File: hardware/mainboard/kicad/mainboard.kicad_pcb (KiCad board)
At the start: 4 copper layers, 54 x 120 mm, 134 parts, among them J1 XT30PW-M, J10 J_PYRO2, J11 J_GPS, J12 J_QWIIC, J13 J_CAM, J14 J_LED, J15 J_EXP, J2 J_BAT1, J3 J_SW, J4 J_ARM, J5 J_SERVO1, J6 J_SERVO2, J7 J_SERVO3, J8 J_MOT, J9 J_PYRO1, Q1 AO3401A, Q2 AO3401A, Q3 AO3400A, Q4 AO3400A, Q5 AO3400A, U1 TPS563201DDCR, U10 E22-400T22S, U2 TPS63070RNMR, U3 AP2112K-3.3TRG1, U4 ICM-42688-P, U5 BMP390, U6 INA219AIDR, U7 DRV8833PWPR, U8 74AHCT1G125, U9 74AHCT1G125

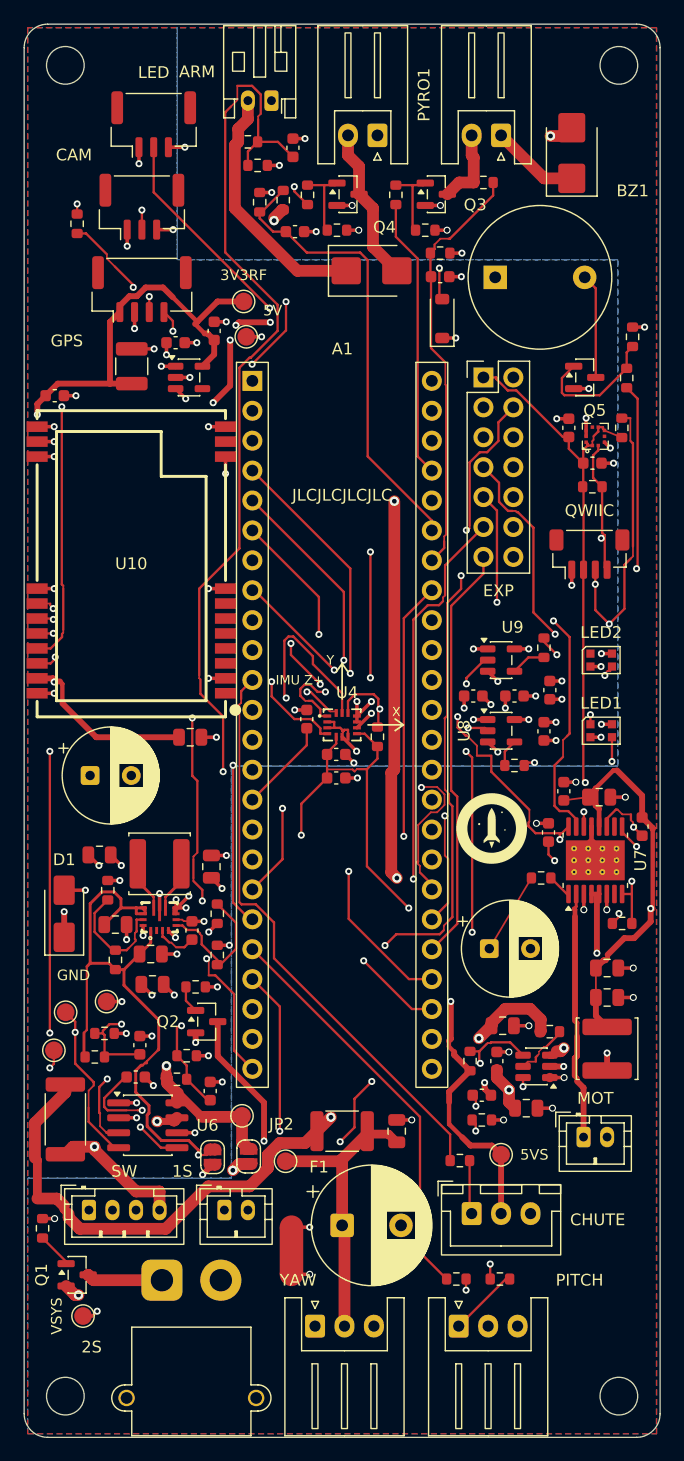
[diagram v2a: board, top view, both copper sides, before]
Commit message: Mainboard rev B1: Review A1-A8 und Entscheidungen E1-E10 eingearbeitet, 2S-Pfad als F.Cu-Flaechen, 28 Verbindungen offen
Schaltung (circuit.py, ERC 0, Netzliste gegen README §4 OK): Hold-up hinter D1, EN-Teiler 330k/115k,
P-FET-Lastschalter je Akku, Polyfuse je Akku, Kelvin-Shunt mit INA239 an SPI1, BMP390 an SPI1,
74HC138/74HC4051 mit gemeinsamer Adresse, J_STACK 2x10 mit LDO 3V3_EXP, 1S-Lader MCP73831,
J_CHG2, vier Pyro-Kanaele (3/4 DNP), vierter Servo, alle Servos und Rollmotor an VSERVO,
3V3_SENS, eine WS2812B-Kette, Summer Pin 37, E22 NRST Pin 6; 166 Bauteile.

Platine (gen_pcb.py): neue Platzierung, 2S-Pfad, Pyro-Ausgaenge und VSYS_IN als F.Cu-Flaechen mit
Sperrflaechen fuer Freerouting, Strom-Klasse nur F.Cu, IMU-Zone 5 mm, patch mit Umweg ueber In2.
DRC 0 Fehler, Paritaet 0, kein 2S-Netz auf In2; 28 offene Verbindungen, Liste in kicad/README.md §5.5.
Spezifikation README.md und kicad/README.md auf B1 nachgezogen, review_check_layout.py fuer B1.

Co-Authored-By: Claude Opus 5.5 <noreply@anthropic.com>
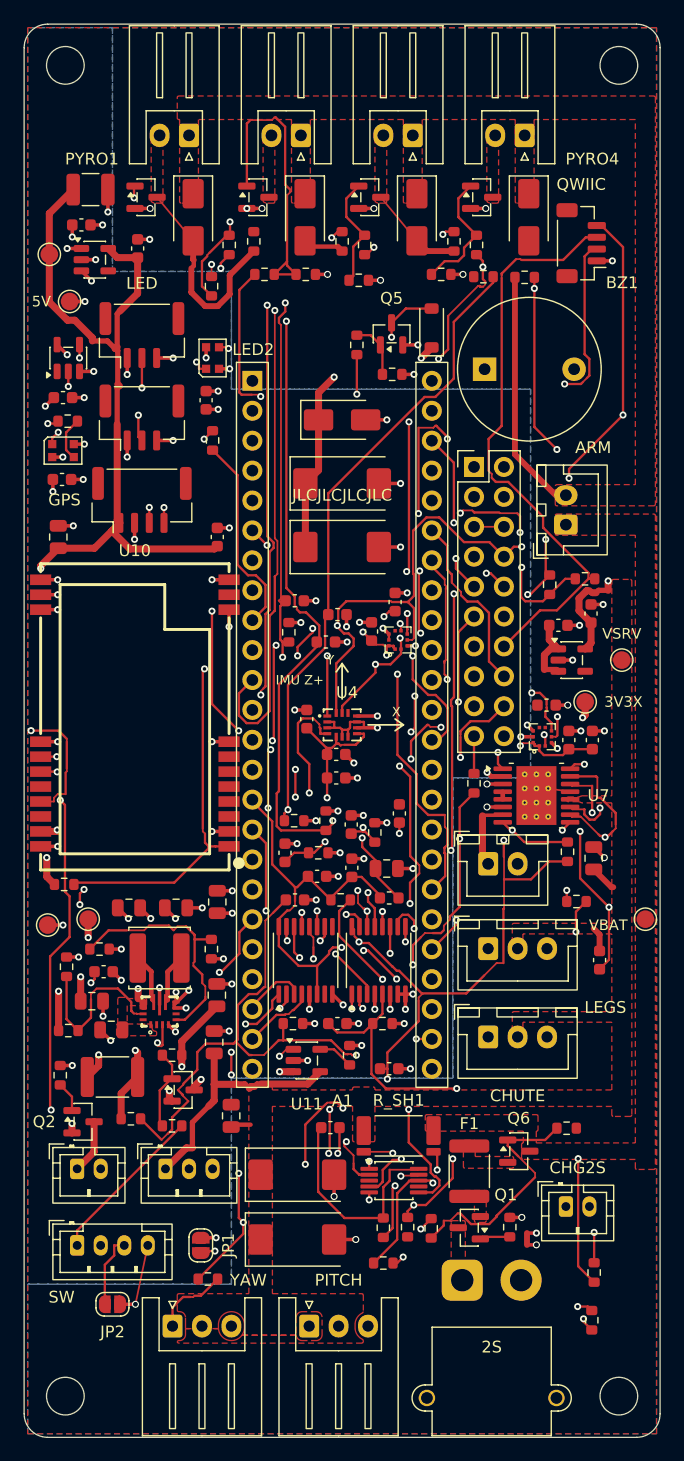
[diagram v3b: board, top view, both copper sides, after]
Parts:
- removed L1: 2.2u Isat>=4A, Inductor_SMD:L_Changjiang_FNR5040S
- removed TP8: SDA, TestPoint:TestPoint_Pad_D1.5mm
- removed TP9: SCL, TestPoint:TestPoint_Pad_D1.5mm
- removed U1: TPS563201DDCR, Package_TO_SOT_SMD:SOT-23-6
- removed U9: 74AHCT1G125, Package_TO_SOT_SMD:SOT-23-5
- added C41: 100n, Capacitor_SMD:C_0603_1608Metric, F.Cu at (125.6, 102.5)
- added C42: 100n, Capacitor_SMD:C_0603_1608Metric, F.Cu at (123.0, 99.0)
- added C43: 100n, Capacitor_SMD:C_0603_1608Metric, F.Cu at (126.6, 100.1)
- added C44: 100n, Capacitor_SMD:C_0603_1608Metric, F.Cu at (103.3, 81.7)
- added C45: 100n, Capacitor_SMD:C_0603_1608Metric, F.Cu at (103.2, 88.7)
- added C46: 100n, Capacitor_SMD:C_0603_1608Metric, F.Cu at (115.5, 81.9)
- added D5: SMAJ12CA, Diode_SMD:D_SMA, F.Cu at (133.3, 66.4)
- added D6: SMAJ12CA, Diode_SMD:D_SMA, F.Cu at (142.8, 66.4)
- added F2: 2A hold, Fuse:Fuse_1812_4532Metric, F.Cu at (107.5, 139.4)
- added FB1: 600R@100MHz, Inductor_SMD:L_0603_1608Metric, F.Cu at (131.0, 124.2)
- added J16: J_SERVO4, Connector_JST:JST_XH_B3B-XH-A_1x03_P2.50mm_Vertical, F.Cu at (139.4, 128.5)
- added J17: J_CHG1, Connector_JST:JST_PH_B3B-PH-K_1x03_P2.00mm_Vertical, F.Cu at (112.0, 147.2)
- added J18: J_CHG2, Connector_JST:JST_PH_B2B-PH-K_1x02_P2.00mm_Vertical, F.Cu at (146.0, 150.4)
- added J19: J_PYRO3, Connector_JST:JST_XH_S2B-XH-A_1x02_P2.50mm_Horizontal, F.Cu at (133.0, 59.4)
- added J20: J_PYRO4, Connector_JST:JST_XH_S2B-XH-A_1x02_P2.50mm_Horizontal, F.Cu at (142.5, 59.4)
- added Q6: AO3401A, Package_TO_SOT_SMD:SOT-23, F.Cu at (142.0, 145.7)
- added Q7: AO3401A, Package_TO_SOT_SMD:SOT-23, F.Cu at (113.5, 140.5)
- added Q8: AO3400A, Package_TO_SOT_SMD:SOT-23, F.Cu at (129.3, 64.7)
- added Q9: AO3400A, Package_TO_SOT_SMD:SOT-23, F.Cu at (138.8, 64.7)
- added R37: 33k, Resistor_SMD:R_0603_1608Metric, F.Cu at (125.6, 117.6)
- added R38: 100, Resistor_SMD:R_0603_1608Metric, F.Cu at (128.9, 68.8)
- added R39: 100k, Resistor_SMD:R_0603_1608Metric, F.Cu at (128.4, 71.8)
- added R40: 100k, Resistor_SMD:R_0603_1608Metric, F.Cu at (136.5, 68.4)
- added R41: 33k, Resistor_SMD:R_0603_1608Metric, F.Cu at (122.5, 101.6)
- added R42: 100, Resistor_SMD:R_0603_1608Metric, F.Cu at (138.4, 68.8)
- added R43: 100k, Resistor_SMD:R_0603_1608Metric, F.Cu at (135.4, 71.2)
- added R44: 100k, Resistor_SMD:R_0603_1608Metric, F.Cu at (139.0, 71.4)
- added R45: 33k, Resistor_SMD:R_0603_1608Metric, F.Cu at (122.9, 117.6)
- added R46: 330, Resistor_SMD:R_0603_1608Metric, F.Cu at (103.7, 83.7)
- added R47: 100, Resistor_SMD:R_0603_1608Metric, F.Cu at (128.2, 77.2)
- added R48: 100k, Resistor_SMD:R_0603_1608Metric, F.Cu at (131.2, 79.7)
- added R49: 1k, Resistor_SMD:R_0603_1608Metric, F.Cu at (116.0, 85.3)
- added U11: MCP73831T-2ACI/OT, Package_TO_SOT_SMD:SOT-23-5, F.Cu at (124.0, 138.0)
- added U12: 74HC138PW, Package_SO:TSSOP-16_4.4x5mm_P0.65mm, F.Cu at (123.9, 129.5)
- added U13: 74HC4051PW, Package_SO:TSSOP-16_4.4x5mm_P0.65mm, F.Cu at (130.1, 129.5)
- added U14: AP2112K-3.3TRG1, Package_TO_SOT_SMD:SOT-23-5, F.Cu at (146.5, 104.0)
- added U15: BMP390, lcsc:LGA-10_L2.0-W2.0-P0.50-BL, F.Cu at (131.8, 102.3)
- C10: value 22u/10V -> 10u/25V
- C11: value 470u/10V -> 10u/25V; footprint Capacitor_THT:CP_Radial_D8.0mm_P3.50mm -> Capacitor_SMD:C_0805_2012Metric
- C13, C14: value 10u/25V -> 22u/10V
- C15: value 100n -> 22u/10V; footprint Capacitor_SMD:C_0603_1608Metric -> Capacitor_SMD:C_0805_2012Metric
- C16, C17: value 22u/10V -> 470u/6.3V polymer; footprint Capacitor_SMD:C_0805_2012Metric -> Capacitor_Tantalum_SMD:CP_EIA-7343-31_Kemet-D
- C18: value 22u/10V -> 1u; footprint Capacitor_SMD:C_0805_2012Metric -> Capacitor_SMD:C_0603_1608Metric
- C19: value 1000u/10V polymer -> 1u; footprint Capacitor_THT:CP_Radial_D8.0mm_P3.50mm -> Capacitor_SMD:C_0603_1608Metric
- C20: value 1u -> 100u/6.3V; footprint Capacitor_SMD:C_0603_1608Metric -> Capacitor_SMD:C_1210_3225Metric
- C22: value 100u/6.3V -> 1u; footprint Capacitor_SMD:C_1210_3225Metric -> Capacitor_SMD:C_0603_1608Metric
- C23: value 100n -> 10u; footprint Capacitor_SMD:C_0603_1608Metric -> Capacitor_SMD:C_0805_2012Metric
- C24: value 2.2u -> 100n
- C25, C32: value 10n -> 100n
- C27, C38: value 100n -> 2.2u
- C28: value 10u -> 10n; footprint Capacitor_SMD:C_0805_2012Metric -> Capacitor_SMD:C_0603_1608Metric
- C3: value 1000u/16V low-ESR -> 100n; footprint Capacitor_THT:CP_Radial_D10.0mm_P5.00mm -> Capacitor_SMD:C_0603_1608Metric
- C30: value 10u/25V -> 100n; footprint Capacitor_SMD:C_0805_2012Metric -> Capacitor_SMD:C_0603_1608Metric
- C33: value 2.2u -> 10u; footprint Capacitor_SMD:C_0603_1608Metric -> Capacitor_SMD:C_0805_2012Metric
- C35: value 100n -> 10u/25V; footprint Capacitor_SMD:C_0603_1608Metric -> Capacitor_SMD:C_0805_2012Metric
- C37: value 100n -> 10n
- C4, C5: value 10u/25V -> 330u/16V polymer; footprint Capacitor_SMD:C_0805_2012Metric -> Capacitor_Tantalum_SMD:CP_EIA-7343-31_Kemet-D
- C8: value 100n -> 4.7u; footprint Capacitor_SMD:C_0603_1608Metric -> Capacitor_SMD:C_0805_2012Metric
- C9: value 22u/10V -> 4.7u
- D2, D3: value SMBJ12CA -> SMAJ12CA; footprint Diode_SMD:D_SMB -> Diode_SMD:D_SMA
- F1: value 3A hold -> 3A hold 6A trip
- J15: value J_EXP -> J_STACK; footprint Connector_PinHeader_2.54mm:PinHeader_2x07_P2.54mm_Vertical -> Connector_PinHeader_2.54mm:PinHeader_2x10_P2.54mm_Vertical
- J4: footprint Connector_JST:JST_PH_S2B-PH-K_1x02_P2.00mm_Horizontal -> Connector_JST:JST_XH_B2B-XH-A_1x02_P2.50mm_Vertical
- J8: footprint Connector_JST:JST_PH_B2B-PH-K_1x02_P2.00mm_Vertical -> Connector_JST:JST_XH_B2B-XH-A_1x02_P2.50mm_Vertical
- NT1: footprint NetTie:NetTie-2_SMD_Pad2.0mm -> NetTie:NetTie-2_SMD_Pad0.5mm
- R10: value 680k -> 1k
- R11: value 130k -> 100k
- R12: value 330k -> 33k
- R13: value 100k -> 2k
- R14: value 10k -> 680k
- R15: value 4.7k -> 130k
- R16: value 4.7k -> 330k
- R17: value 220 -> 115k
- R18, R19: value 220 -> 10k
- R20, R21: value 10k -> 4.7k
- R22, R8: value 100k -> 10k
- R23: value 33k -> 220
- R24: value 100 -> 220
- R25, R26: value 100k -> 220
- R27: value 33k -> 10k
- R28: value 100 -> 100k
- R29: value 100k -> 33k
- R3: value 33k -> 1k
- R30: value 100k -> 100
- R31, R9: value 33k -> 100k
- R32: value 330 -> 100k
- R33: value 330 -> 33k
- R36: value 1k -> 100k
- R5: value 56k -> 33k
- R6, R7: value 10k -> 10
- R_SH1: footprint Resistor_SMD:R_2512_6332Metric -> mainboard:R_2512_Kelvin
- TP5: value 5V_SERVO -> 3V3_RF
- TP6: value 3V3_RF -> 3V3_EXP
- U6: value INA219AIDR -> INA239AIDGSR; footprint Package_SO:SOIC-8_3.9x4.9mm_P1.27mm -> Package_SO:MSOP-10_3x3mm_P0.5mm
- U8: value 74AHCT1G125 -> SN74LV1T34DBVR
- moved R24 97.0 mm to (148.2, 160.1)
- moved R23 94.7 mm to (115.6, 156.6)
- moved R25 89.7 mm to (148.4, 156.0), turned to 90 degrees
- moved TP5 85.5 mm to (102.1, 69.5)
- moved R22 65.0 mm to (103.4, 123.0)
- moved R16 64.1 mm to (103.8, 135.5)
- moved R15 62.7 mm to (106.4, 128.5), turned to 0 degrees
- moved R26 61.6 mm to (146.9, 124.5)
- moved C18 53.5 mm to (104.9, 67.0)
- moved R29 52.9 mm to (125.0, 120.4)
- moved C29 52.5 mm to (146.2, 110.8), turned to 90 degrees
- moved R27 52.0 mm to (146.1, 120.3), turned to 90 degrees
- moved LED1 51.5 mm to (103.3, 86.2)
- moved TP4 51.2 mm to (150.8, 104.0)
- moved C35 51.1 mm to (148.4, 120.8), turned to 90 degrees
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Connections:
- net LED1_DATA renamed LED_DATA
- A1 pad 12: EXP_D10 -> SERVO_LEGS
- A1 pad 13: EXP_D11 -> MOT_NSLEEP
- A1 pad 14: EXP_D12 -> PYRO3_FIRE
- A1 pad 16: ARM_SENSE -> MUX_OUT
- A1 pad 17: EXP_D25 -> SEL1
- A1 pad 18: IMU_MOSI -> SPI1_MOSI
- A1 pad 19: IMU_SCK -> SPI1_SCK
- A1 pad 22: EXP_D30 -> SEL2
- A1 pad 23: EXP_D31 -> CS_EN
- A1 pad 30: PYRO2_SENSE -> EXT_RX
- A1 pad 31: PYRO1_SENSE -> EXT_TX
- A1 pad 34: EXP_D17 -> IRQ_EXT
- A1 pad 35: EXP_D16 -> unconnected-(A1-D16-Pad35)
- A1 pad 36: EXP_D15 -> NRST_EXT
- A1 pad 37: EXP_D14 -> PYRO4_FIRE
- A1 pad 38: BUZZER -> PWM_EXT
- A1 pad 40: VBAT1_SENSE -> unconnected-(A1-D41-Pad40)
- A1 pad 41: VBAT2_SENSE -> unconnected-(A1-D40-Pad41)
- A1 pad 42: IMU_MISO -> SPI1_MISO
- A1 pad 43: IMU_CS -> SEL0
- A1 pad 44: EXP_D37 -> BUZZER
- A1 pad 8: LED2_DATA -> LORA_NRST
- C10 pad 1: 5V_SERVO -> VSYS_IN
- C10 pad 2: GND_PWR -> GND
- C11 pad 1: 5V_SERVO -> VSYS_IN
- C11 pad 2: GND_PWR -> GND
- C12 pad 1: VBAT1_SENSE -> U2_VAUX
- C13 pad 1: VSYS_IN -> 5V_SYS
- C14 pad 1: VSYS_IN -> 5V_SYS
- C15 pad 1: U2_VAUX -> 5V_SYS
- C16 pad 1: 5V_SYS -> TEENSY_VIN
- C17 pad 1: 5V_SYS -> TEENSY_VIN
- C19 pad 1: 5V_SYS -> 3V3_RF
- C2 pad 1: 3V3 -> INA_INP
- C2 pad 2: GND -> INA_INN
- C20 pad 1: 5V_SYS -> 3V3_RF
- C21 pad 1: 3V3_RF -> 5V_SYS
- C22 pad 1: 3V3_RF -> 3V3_EXP
- C23 pad 1: 3V3 -> 3V3_SENS
- C26 pad 1: 3V3 -> 3V3_SENS
- C27 pad 1: 3V3 -> 3V3_SENS
- C28 pad 1: 3V3_RF -> 3V3_SENS
- C29 pad 1: 3V3_RF -> 3V3_SENS
- C3 pad 1: VSERVO -> 3V3
- C3 pad 2: GND_PWR -> GND
- C30 pad 1: 5V_SERVO -> 3V3_SENS
- C30 pad 2: GND_PWR -> GND
- C31 pad 1: 5V_SERVO -> 3V3_SENS
- C31 pad 2: GND_PWR -> GND
- C32 pad 1: U7_VCP -> 3V3_SENS
- C32 pad 2: 5V_SERVO -> GND
- C33 pad 1: U7_VINT -> 3V3_RF
- C33 pad 2: GND_PWR -> GND
- C34 pad 1: ARM_SENSE -> 3V3_RF
- C35 pad 1: PYRO1_SENSE -> VSERVO
- C35 pad 2: GND -> GND_PWR
- C36 pad 1: PYRO2_SENSE -> VSERVO
- C36 pad 2: GND -> GND_PWR
- C37 pad 1: 5V_SYS -> U7_VCP
- C37 pad 2: GND -> VSERVO
- C38 pad 1: 5V_SYS -> U7_VINT
- C38 pad 2: GND -> GND_PWR
- C39 pad 1: 5V_SYS -> ARM_SENSE
- C40 pad 1: 5V_SYS -> PYRO1_SENSE
- C5 pad 1: VBAT_MEAS -> VSERVO
- C6 pad 1: VBAT_MEAS -> VSERVO
- C7 pad 1: VBAT_MEAS -> VBAT1_SENSE
- C7 pad 2: GND_PWR -> GND
- C8 pad 1: U1_BST -> VBUS_CHG
- C8 pad 2: U1_SW -> GND
- C9 pad 1: 5V_SERVO -> VBAT1_F
- C9 pad 2: GND_PWR -> GND
- F1 pad 1: VBAT_MEAS -> VBAT2_REV
- F1 pad 2: VSERVO -> VBAT2_F
- J15 pad 1: 3V3 -> GND
- J15 pad 10: EXP_D25 -> CS_EXT0
- J15 pad 11: EXP_D30 -> CS_EXT1
- J15 pad 12: EXP_D31 -> CS_EXT2
- J15 pad 13: EXP_D37 -> IRQ_EXT
- J15 pad 14: 5V_SYS -> SDA
- J15 pad 2: GND -> GND_PWR
- J15 pad 3: EXP_D10 -> 3V3_EXP
- J15 pad 4: EXP_D11 -> 5V_SYS
- J15 pad 5: EXP_D12 -> VSERVO
- J15 pad 6: EXP_D14 -> VSERVO
- J15 pad 7: EXP_D15 -> SPI1_SCK
- J15 pad 8: EXP_D16 -> SPI1_MOSI
- J15 pad 9: EXP_D17 -> SPI1_MISO
- J3 pad 1: VBAT1_PROT -> SW1_G
- J3 pad 2: VSYS_IN -> GND
- J3 pad 3: VBAT2_REV -> SW2_G
- J3 pad 4: VBAT_PROT -> GND_PWR
- J7 pad 2: 5V_SERVO -> VSERVO
- JP1 pad 1: VBAT1_PROT -> SW1_G
- JP1 pad 2: VSYS_IN -> GND
- JP2 pad 1: VBAT2_REV -> SW2_G
- JP2 pad 2: VBAT_PROT -> GND_PWR
- LED1 pad 1: LED_EXT_DATA -> LED2_DIN
- LED2 pad 1: unconnected-(LED2-DOUT-Pad1) -> LED_EXT_DATA
- Q2 pad 2: VBAT1_PROT -> VBAT1_REV
- R10 pad 1: 5V_SYS -> Q7_G
- R10 pad 2: U2_FB -> SW1_G
- R11 pad 1: U2_FB -> VBAT1_F
- R11 pad 2: GND -> VBAT1_SENSE
- R12 pad 1: VSYS_IN -> VBAT1_SENSE
- R12 pad 2: U2_EN -> GND
- R13 pad 1: U2_EN -> CHG_PROG
- R14 pad 1: 3V3 -> 5V_SYS
- R14 pad 2: IMU_CS -> U2_FB
- R15 pad 1: 3V3 -> U2_FB
- R15 pad 2: SDA -> GND
- R16 pad 1: 3V3 -> VSYS_IN
- R16 pad 2: SCL -> U2_EN
- R17 pad 1: SERVO_YAW -> U2_EN
- R17 pad 2: SERVO_YAW_S -> GND
- R18 pad 1: SERVO_PITCH -> 3V3
- R18 pad 2: SERVO_PITCH_S -> CS_EN
- R19 pad 1: SERVO_CHUTE -> ARM_SENSE
- R19 pad 2: SERVO_CHUTE_S -> ARM_EXT
- R2 pad 1: VBAT_PROT -> Q6_G
- R2 pad 2: VBAT2_SENSE -> VBAT2_F
- R20 pad 1: 5V_SERVO -> 3V3
- R20 pad 2: U7_SLEEP -> SDA
- R21 pad 2: MOT_FAULT -> SCL
- R22 pad 1: VBAT_ARMED -> 3V3_RF
- R22 pad 2: ARM_SENSE -> LORA_NRST
- R23 pad 1: ARM_SENSE -> SERVO_YAW
- R23 pad 2: GND -> SERVO_YAW_S
- R24 pad 1: PYRO1_FIRE -> SERVO_PITCH
- R24 pad 2: PYRO1_G -> SERVO_PITCH_S
- R25 pad 1: PYRO1_G -> SERVO_CHUTE
- R25 pad 2: GND_PWR -> SERVO_CHUTE_S
- R26 pad 1: PYRO1_NEG -> SERVO_LEGS
- R26 pad 2: PYRO1_SENSE -> SERVO_LEGS_S
- R27 pad 1: PYRO1_SENSE -> 3V3
- R27 pad 2: GND -> MOT_FAULT
- R28 pad 1: PYRO2_FIRE -> VBAT_ARMED
- R28 pad 2: PYRO2_G -> ARM_SENSE
- R29 pad 1: PYRO2_G -> ARM_SENSE
- R29 pad 2: GND_PWR -> GND
- R3 pad 1: VBAT2_SENSE -> Q6_G
- R3 pad 2: GND -> SW2_G
- R30 pad 1: PYRO2_NEG -> PYRO1_FIRE
- R30 pad 2: PYRO2_SENSE -> PYRO1_G
- R31 pad 1: PYRO2_SENSE -> PYRO1_G
- R31 pad 2: GND -> GND_PWR
- R32 pad 1: LED1_5V -> PYRO1_NEG
- R32 pad 2: LED1_DIN -> PYRO1_SENSE
- R33 pad 1: LED2_5V -> PYRO1_SENSE
- R33 pad 2: LED2_DIN -> GND
- R34 pad 1: BUZZER -> PYRO2_FIRE
- R34 pad 2: BZ_G -> PYRO2_G
- R35 pad 1: BZ_G -> PYRO2_G
- R35 pad 2: GND -> GND_PWR
- R36 pad 1: CAM_TRIG -> PYRO2_NEG
- R36 pad 2: CAM_TRIG_OUT -> PYRO2_SENSE
- R4 pad 1: VBAT_MEAS -> VBAT2_F
- R4 pad 2: U1_EN -> VBAT2_SENSE
- R5 pad 1: 5V_SERVO -> VBAT2_SENSE
- R5 pad 2: U1_FB -> GND
- R6 pad 1: U1_FB -> ISENS_P
- R6 pad 2: GND_PWR -> INA_INP
- R7 pad 1: Q2_G -> ISENS_N
- R7 pad 2: GND -> INA_INN
- R8 pad 1: VSYS_IN -> Q2_G
- R8 pad 2: VBAT1_SENSE -> GND
- R9 pad 1: VBAT1_SENSE -> Q7_G
- R9 pad 2: GND -> VBAT1_F
- R_SH1 pad 2: VBAT_MEAS -> ISENS_P
- TP5 pad 1: 5V_SERVO -> 3V3_RF
- TP6 pad 1: 3V3_RF -> 3V3_EXP
- U10 pad 1: unconnected-(U10-RESET-Pad1) -> LORA_NRST
- U2 pad 6: GND -> unconnected-(U2-FB2-Pad6)
- U4 pad 1: IMU_MISO -> SPI1_MISO
- U4 pad 12: IMU_CS -> CS_IMU
- U4 pad 13: IMU_SCK -> SPI1_SCK
- U4 pad 14: IMU_MOSI -> SPI1_MOSI
- U4 pad 5: 3V3 -> 3V3_SENS
- U4 pad 8: 3V3 -> 3V3_SENS
- U5 pad 1: 3V3 -> 3V3_SENS
- U5 pad 10: 3V3 -> 3V3_SENS
- U5 pad 2: SCL -> SPI1_SCK
- U5 pad 4: SDA -> SPI1_MOSI
- U5 pad 5: 3V3 -> SPI1_MISO
- U5 pad 6: 3V3 -> CS_BARO
- U6 pad 1: GND -> CS_INA
- U6 pad 2: GND -> SPI1_MOSI
- U6 pad 3: SDA -> unconnected-(U6-~{ALERT}-Pad3)
- U6 pad 4: SCL -> SPI1_MISO
- U6 pad 5: 3V3 -> SPI1_SCK
- U6 pad 6: GND -> 3V3
- U6 pad 7: VBAT_MEAS -> GND
- U6 pad 8: VBAT_PROT -> ISENS_N
- U7 pad 1: U7_SLEEP -> MOT_NSLEEP
- U7 pad 12: 5V_SERVO -> VSERVO
- U8 pad 1: GND -> unconnected-(U8-NC-Pad1)
- U8 pad 4: LED1_5V -> LED_5V
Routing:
- net SPI1_MOSI: track 0.00 -> 155.2 mm, vias 0 -> 6
- net VBAT_PROT: track 138.4 -> 0.00 mm, vias 4 -> 0
- net SPI1_MISO: track 0.00 -> 110.5 mm, vias 0 -> 8
- net LORA_AUX: track 109.7 -> 0.00 mm, vias 2 -> 0
- net SPI1_SCK: track 0.00 -> 109.6 mm, vias 0 -> 11
- net VBAT_MEAS: track 107.8 -> 0.00 mm, vias 5 -> 0
- net SDA: track 162.6 -> 57.0 mm, vias 8 -> 0
- net 5V_SERVO: track 104.6 -> 0.00 mm, vias 2 -> 0
- net SERVO_CHUTE: track 49.4 -> 151.8 mm, vias 0 -> 2
- net LORA_M0: track 176.7 -> 76.6 mm, vias 1 -> 3
- net PYRO3_SENSE: track 0.00 -> 87.0 mm, vias 0 -> 4
- net LORA_RXD: track 73.8 -> 0.00 mm, vias 4 -> 0
- net PYRO4_SENSE: track 0.00 -> 68.7 mm, vias 0 -> 2
- net LED_EXT_DATA: track 77.2 -> 9.35 mm
- net 3V3_SENS: track 0.00 -> 67.8 mm, vias 0 -> 6
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- added copper zone on F.Cu, net PYRO1_NEG
- added copper zone on F.Cu, net PYRO2_NEG
- added copper zone on F.Cu, net PYRO3_NEG
- added copper zone on F.Cu, net PYRO4_NEG
- added copper zone on F.Cu, net VBAT2_F
- added copper zone on F.Cu, net VBAT2_RAW
- added copper zone on F.Cu, net VBAT2_REV
- added copper zone on F.Cu, net VBAT_ARMED
- added copper zone on F.Cu, net VBAT_PROT
- added copper zone on F.Cu, net VSERVO
- added copper zone on F.Cu, net VSYS_IN
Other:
- board text added: "1:GND 2:GNDP 3:3V3 4:5V 5,6:VSRV"
- board text added: "1S GND 2S GNDP"
- board text added: "3V3X"
- board text added: "CHG2S"
- board text added: "J15 STACK"
- board text added: "J16 LEGS"
- board text added: "J17 CHG1S"
- board text added: "J18 CHG2S"
- board text added: "J19 PYRO3"
- board text added: "J20 PYRO4"
- board text added: "LEGS"
- board text added: "PYRO4"
- board text added: "VBAT"
- board text added: "VBUS GND LED"
- board text added: "VSRV"
- board text removed: "1:3V3 2:GND 14:5V"
- board text removed: "1S"
- board text removed: "1S 1S 2S 2S"
- board text removed: "3V3RF"
- board text removed: "5VS"
- board text removed: "CAM"
- board text removed: "EXP"
- board text removed: "GND"
- board text removed: "J15 EXP"
- board text removed: "MOT"
- board text removed: "S 5V -"
- board text removed: "VSYS"

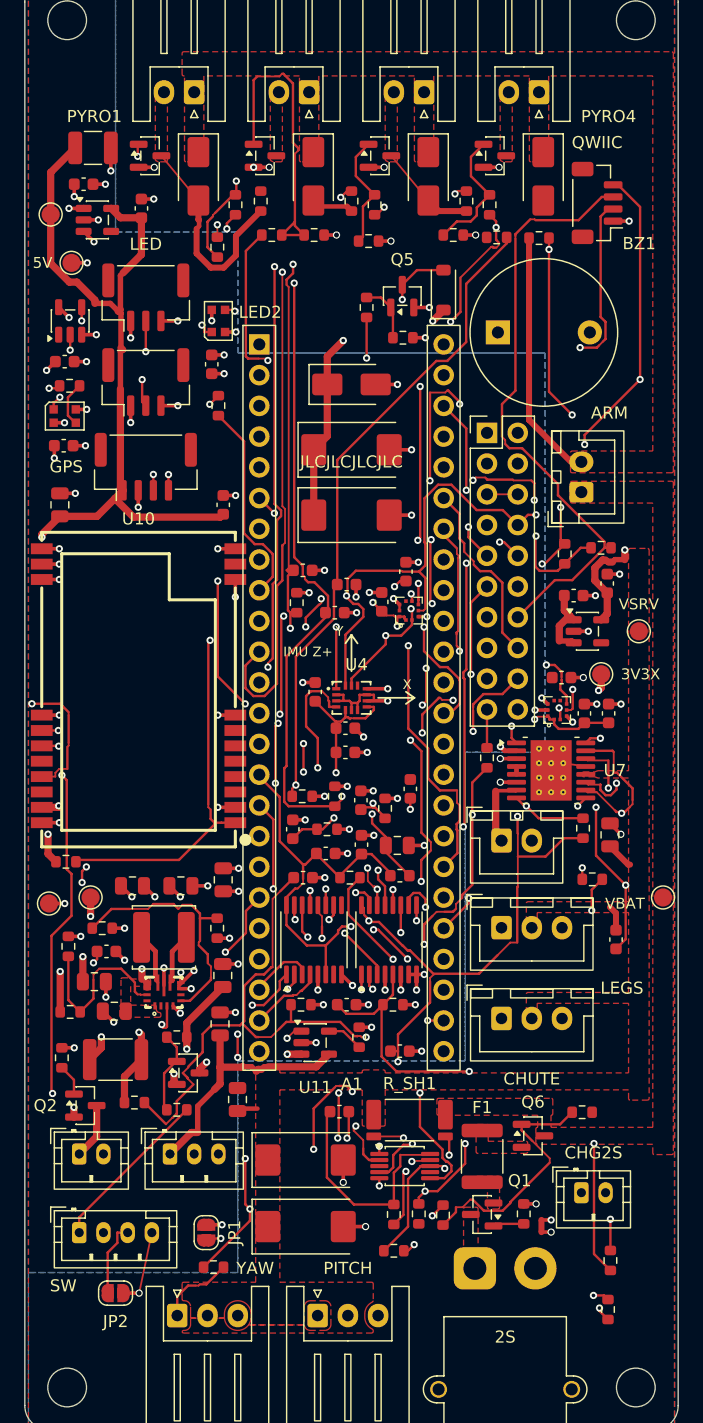
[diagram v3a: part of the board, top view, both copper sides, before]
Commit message: Platine rev B1: Routing-Kette repariert, Skript-Router für die Reste, 21 offene Verbindungen
Kette (make.sh, gen_pcb.py): alles auf der Platine für Freerouting fix exportiert, SES durch
Zusammenführen statt Ersetzen übernommen, Nachläufe auf vier Pässe, IMU-Via-Verbot als Polygon mit
Löchern um die eigenen Masse-Vias, Patch-Schritt mit 0,2 mm Abstand; ein Lauf 25 statt 40 Minuten.
Zwei verworfene Varianten (Power-Lagen als Signallagen, angebundene Pads ohne Netz) im Kommentar.

Neu: gaps.py (offene Verbindungen mit Lage), close_gaps.py (Geometrie-Export, Übernahme) und
route_gaps.py (A*-Gitterrouter 0,05 mm mit Rip-up von Signalbahnen). Damit sechs der 27 Reste
geschlossen; die übrigen 21 (README §5.5 mit Koordinaten) sind in KiCad von Hand zu ziehen.
Stand: DRC 0 Fehler, Parität 0, kein 2S-Netz auf In2, Renders neu.

Co-Authored-By: Claude Fable 5.1 <noreply@anthropic.com>
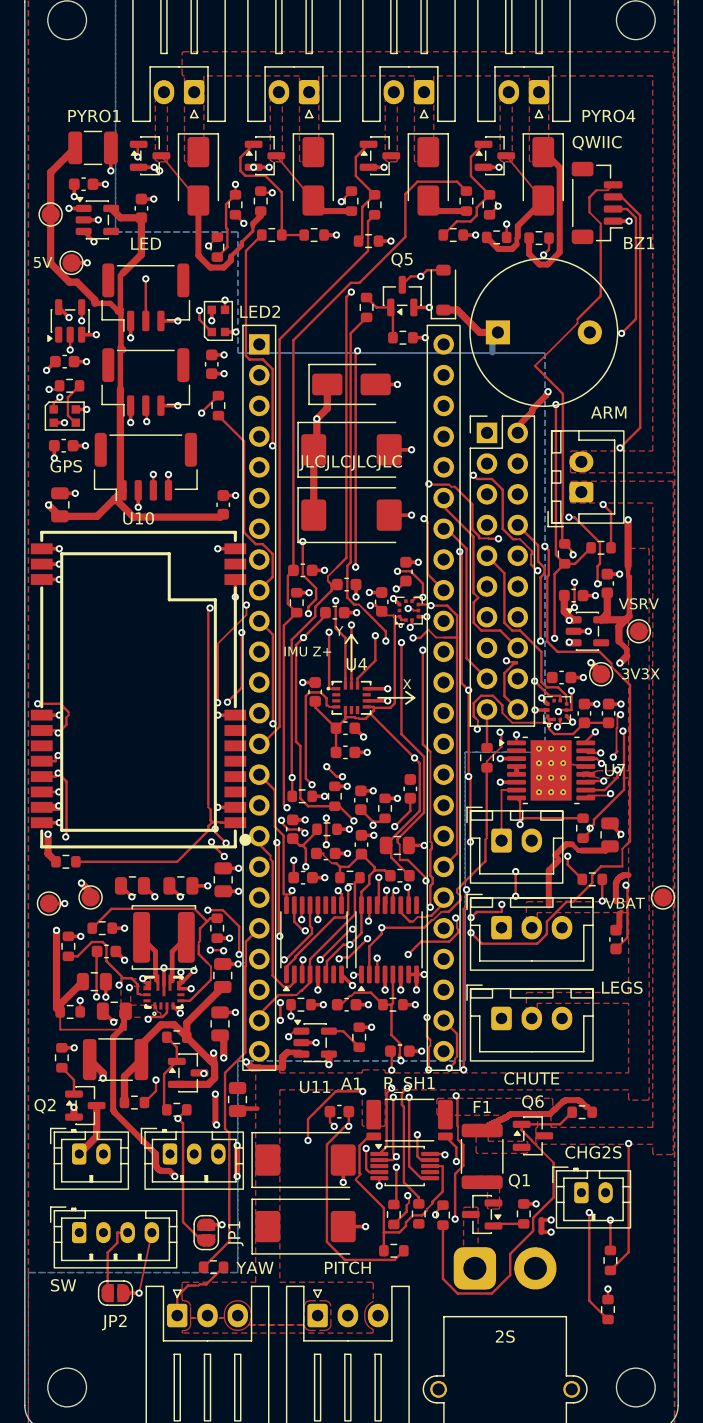
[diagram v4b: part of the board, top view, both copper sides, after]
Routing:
- net PYRO1_SENSE: track 16.6 -> 121.9 mm, vias 2 -> 5
- net CS_BARO: track 2.83 -> 102.5 mm, vias 1 -> 10
- net LORA_RXD: track 0.00 -> 91.7 mm, vias 0 -> 7
- net CS_EXT2: track 0.00 -> 70.0 mm, vias 0 -> 3
- net LORA_AUX: track 0.00 -> 55.2 mm, vias 0 -> 7
- net CS_IMU: track 1.22 -> 54.9 mm, vias 1 -> 8
- net CS_EXT0: track 43.8 -> 0.00 mm, vias 4 -> 0
- net SERVO_LEGS: track 0.95 -> 42.8 mm
- net CS_EXT1: track 41.2 -> 0.00 mm, vias 6 -> 0
- net SERVO_CHUTE: track 151.8 -> 112.2 mm, vias 2 -> 1
- net LORA_M1: track 34.4 -> 0.00 mm, vias 1 -> 0
- net VSYS_IN: track 30.9 -> 58.9 mm, vias 5 -> 10
- net SPI1_MOSI: track 155.2 -> 128.8 mm, vias 6 -> 7
- net LORA_M0: track 76.6 -> 99.9 mm, vias 3 -> 4
- net BUZZER: track 79.1 -> 56.3 mm, vias 2 -> 3
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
